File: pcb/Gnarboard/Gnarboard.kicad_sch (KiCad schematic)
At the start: 11 parts, among them J2 I2C, J3 Screw_Terminal_01x12, J4 Screw_Terminal_01x12, U2 MCP3208, U4 D24V5F3

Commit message: bill of materials updated.
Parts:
- C1: Vendor (none) -> 08053C104KAT4A
- D1: Vendor (none) -> 771-BZT52H-A30-QX
- DFR0570: renamed from U3; Vendor (none) -> 426-DFR0570
- J2: Vendor (none) -> 485-4328
- J3, J4: Vendor (none) -> BSS 2301
- JP1, JP2, U4: now left out of the parts list
- U1: value ~ -> ESP32-DEVKITC; Vendor (none) -> 356-ESP32-DEVKITC32E
- U2: Vendor (none) -> MCP3208T-BI/SL
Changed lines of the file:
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@@
   )
   (symbol (lib_id "Jumper:SolderJumper_2_Bridged") (at 34.29 73.66 0) (unit 1)
-    (in_bom yes) (on_board yes) (dnp no) (fields_autoplaced)
+    (in_bom no) (on_board yes) (dnp no) (fields_autoplaced)
     (property "Reference" "JP2" (at 34.29 67.31 0)
       (effects (font (size 1.27 1.27)))
@@
     )
     (property "Datasheet" "~" (at 95.25 35.56 0)
+      (effects (font (size 1.27 1.27)) hide)
+    )
+    (property "Vendor" "08053C104KAT4A" (at 95.25 35.56 0)
       (effects (font (size 1.27 1.27)) hide)
     )
@@
     )
     (property "Datasheet" "http://ww1.microchip.com/downloads/en/DeviceDoc/21298c.pdf" (at 207.01 59.69 0)
+      (effects (font (size 1.27 1.27)) hide)
+    )
+    (property "Vendor" "MCP3208T-BI/SL" (at 209.55 62.23 0)
       (effects (font (size 1.27 1.27)) hide)
     )
@@
       (effects (font (size 1.27 1.27)) hide)
     )
+    (property "Vendor" "771-BZT52H-A30-QX" (at 52.07 35.56 0)
+      (effects (font (size 1.27 1.27)) hide)
+    )
     (pin "1")
     (pin "2")
@@
     )
     (property "Datasheet" "~" (at 22.86 120.65 0)
+      (effects (font (size 1.27 1.27)) hide)
+    )
+    (property "Vendor" "BSS 2301" (at 22.86 120.65 0)
       (effects (font (size 1.27 1.27)) hide)
     )
@@
   )
   (symbol (lib_id "Jumper:SolderJumper_2_Bridged") (at 50.8 73.66 0) (unit 1)
-    (in_bom yes) (on_board yes) (dnp no) (fields_autoplaced)
+    (in_bom no) (on_board yes) (dnp no) (fields_autoplaced)
     (property "Reference" "JP1" (at 50.8 67.31 0)
       (effects (font (size 1.27 1.27)))
@@
   (symbol (lib_id "gnarboard:DFR0571") (at 74.93 35.56 0) (unit 1)
     (in_bom yes) (on_board yes) (dnp no) (fields_autoplaced)
-    (property "Reference" "U3" (at 74.93 25.4 0)
+    (property "Reference" "DFR0570" (at 74.93 25.4 0)
       (effects (font (size 1.27 1.27)))
     )
@@
     )
     (property "Datasheet" "" (at 74.93 26.67 0)
+      (effects (font (size 1.27 1.27)) hide)
+    )
+    (property "Vendor" "426-DFR0570 " (at 74.93 35.56 0)
       (effects (font (size 1.27 1.27)) hide)
     )
@@
       (project "Gnarboard"
         (path "/c83c6236-96e9-46ad-9d7a-9e2efa4a7966"
-          (reference "U3") (unit 1)
+          (reference "DFR0570") (unit 1)
         )
       )
@@
     )
     (property "Datasheet" "~" (at 22.86 156.21 0)
+      (effects (font (size 1.27 1.27)) hide)
+    )
+    (property "Vendor" "BSS 2301" (at 22.86 156.21 0)
       (effects (font (size 1.27 1.27)) hide)
     )
@@
       (effects (font (size 1.27 1.27)) hide)
     )
+    (property "Vendor" "485-4328" (at 271.78 54.61 0)
+      (effects (font (size 1.27 1.27)) hide)
+    )
     (pin "1")
     (pin "2")
@@
   )
   (symbol (lib_id "gnarboard:ESP32_DevKit_C") (at 156.21 66.04 0) (unit 1)
-    (in_bom yes) (on_board yes) (dnp no) (fields_autoplaced)
+    (in_bom yes) (on_board yes) (dnp no)
     (property "Reference" "U1" (at 156.21 38.1 0)
       (effects (font (size 1.27 1.27)))
     )
-    (property "Value" "~" (at 156.21 39.37 0)
-      (effects (font (size 1.27 1.27)))
+    (property "Value" "ESP32-DEVKITC" (at 156.21 41.91 0)
+      (effects (font (size 1.27 1.27)) hide)
     )
     (property "Footprint" "PCM_Espressif:ESP32-DevKitC" (at 156.21 39.37 0)
@@
     )
     (property "Datasheet" "" (at 156.21 39.37 0)
+      (effects (font (size 1.27 1.27)) hide)
+    )
+    (property "Vendor" "356-ESP32-DEVKITC32E " (at 156.21 66.04 0)
       (effects (font (size 1.27 1.27)) hide)
     )
@@
   )
   (symbol (lib_id "gnarboard:DF24V5Fx") (at 74.93 57.15 0) (unit 1)
-    (in_bom yes) (on_board yes) (dnp no) (fields_autoplaced)
+    (in_bom no) (on_board yes) (dnp no) (fields_autoplaced)
     (property "Reference" "U4" (at 74.93 49.53 0)
       (effects (font (size 1.27 1.27)))

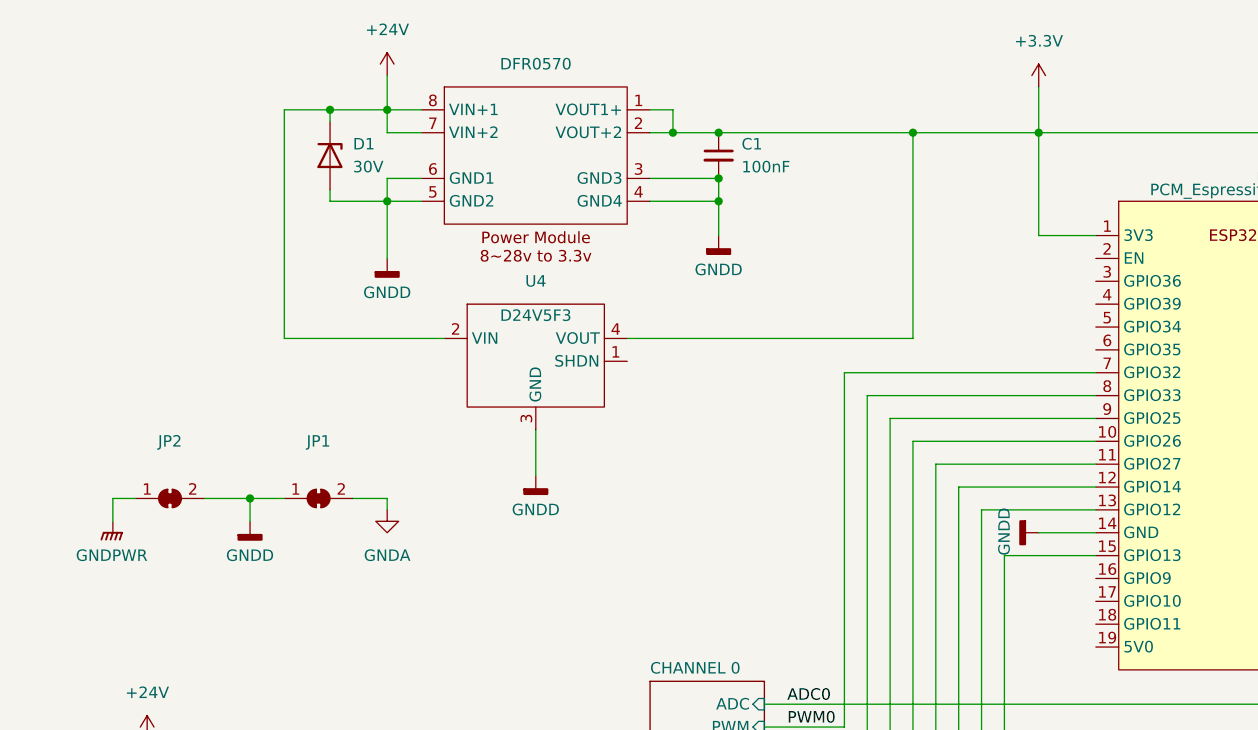
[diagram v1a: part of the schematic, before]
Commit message: added bus voltage reading functionality
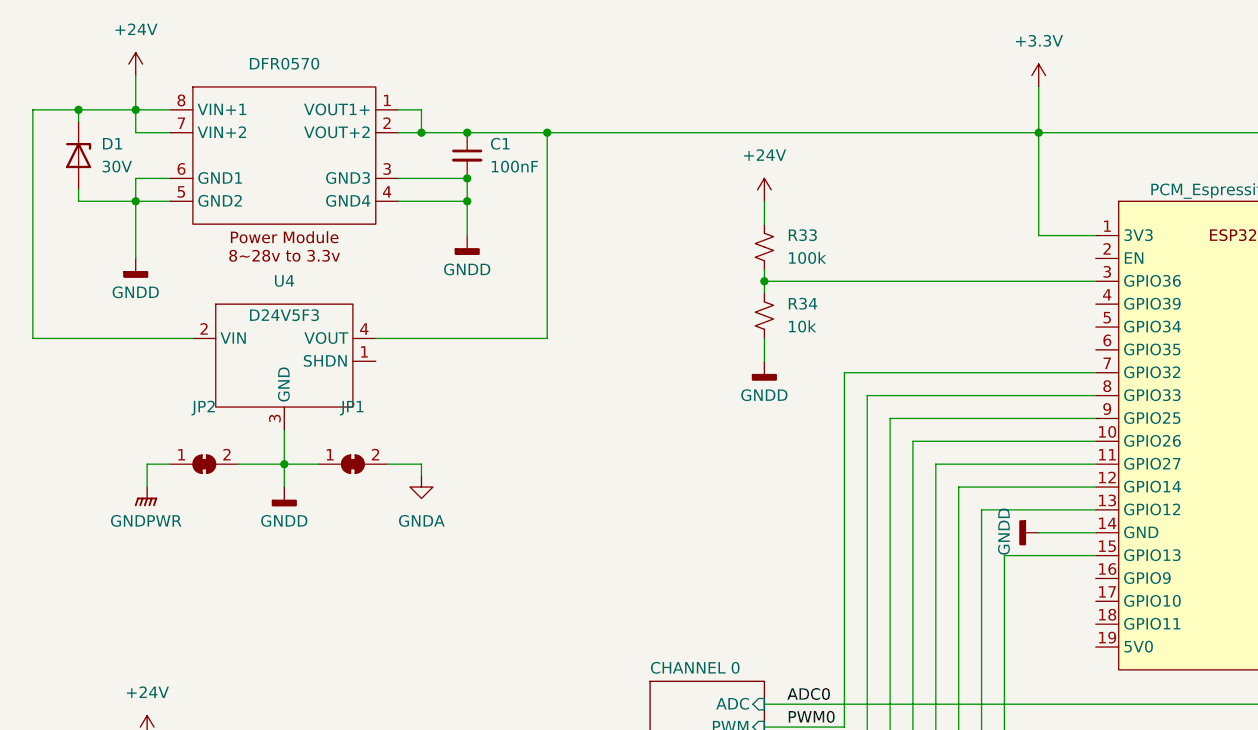
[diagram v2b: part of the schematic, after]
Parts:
- added R33: 100k, Resistor_SMD:R_0805_2012Metric_Pad1.20x1.40mm_HandSolder, symbol Device:R_Small_US
- added R34: 10k, Resistor_SMD:R_0805_2012Metric_Pad1.20x1.40mm_HandSolder, symbol Device:R_Small_US
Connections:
- net +24V: now also R33.2
- net GNDD: now also R34.1
- net at U1.3 (GPIO36): now also R33.1, R34.2
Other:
- moved on the sheet: C1, D1, DFR0570, JP1, JP2, U4

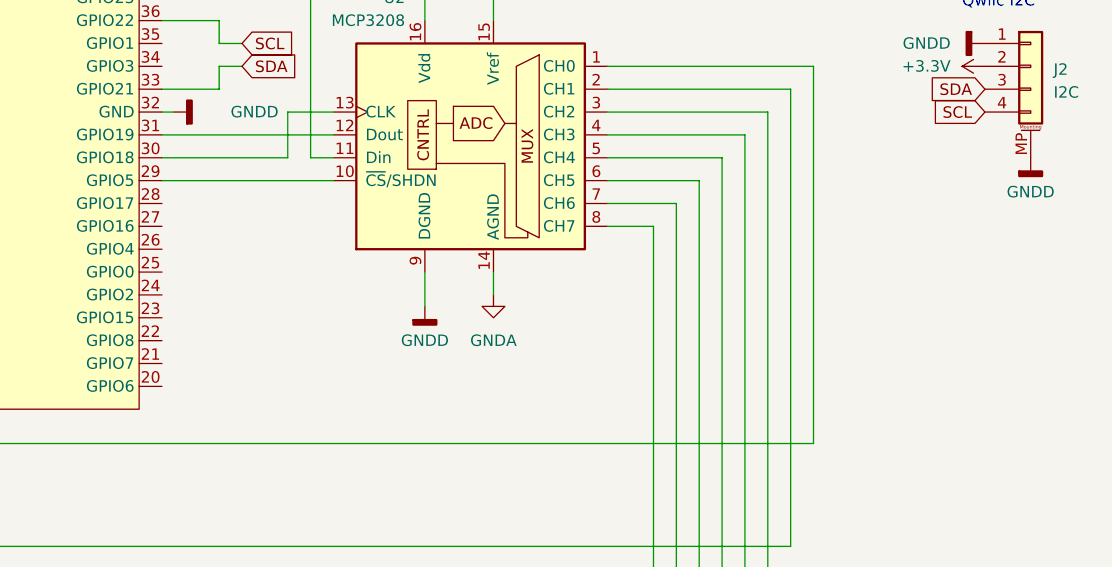
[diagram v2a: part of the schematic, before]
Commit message: got the mosfet driver circuit sorted - zener to the rescue.  also added the CAN/N2K header.
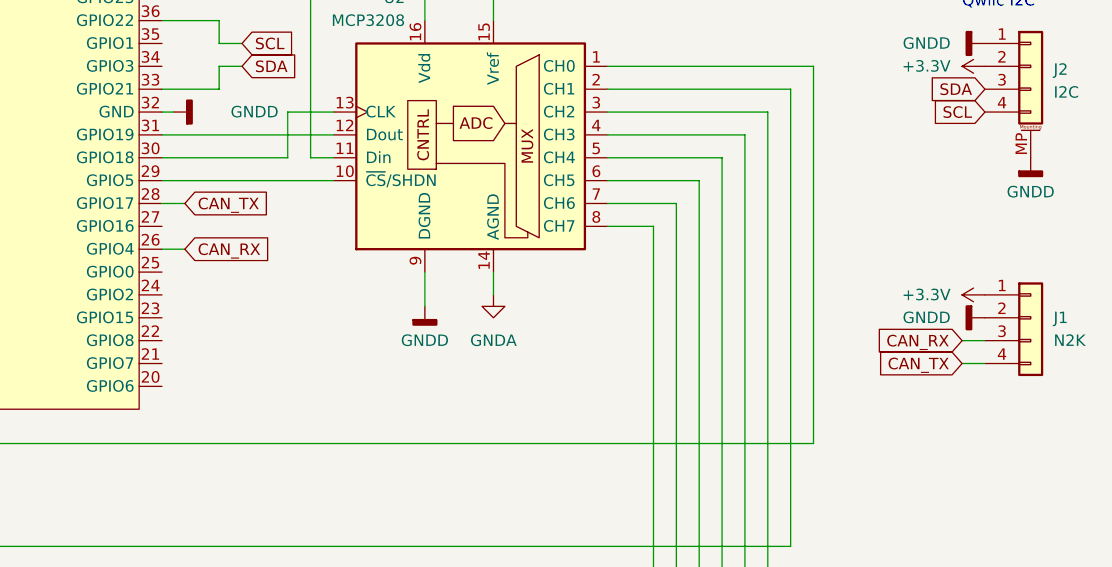
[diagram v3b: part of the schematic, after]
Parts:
- added J1: N2K, Connector_PinSocket_2.54mm:PinSocket_1x04_P2.54mm_Vertical, symbol Connector_Generic:Conn_01x04
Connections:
- net +3.3V: now also J1.1 (Pin_1)
- net GNDD: now also J1.2 (Pin_2)
- net CAN_RX: now reaches U1.26 (GPIO4)
- net CAN_RX: now also J1.3 (Pin_3)
- net CAN_TX: now reaches U1.28 (GPIO17)
- net CAN_TX: now also J1.4 (Pin_4)

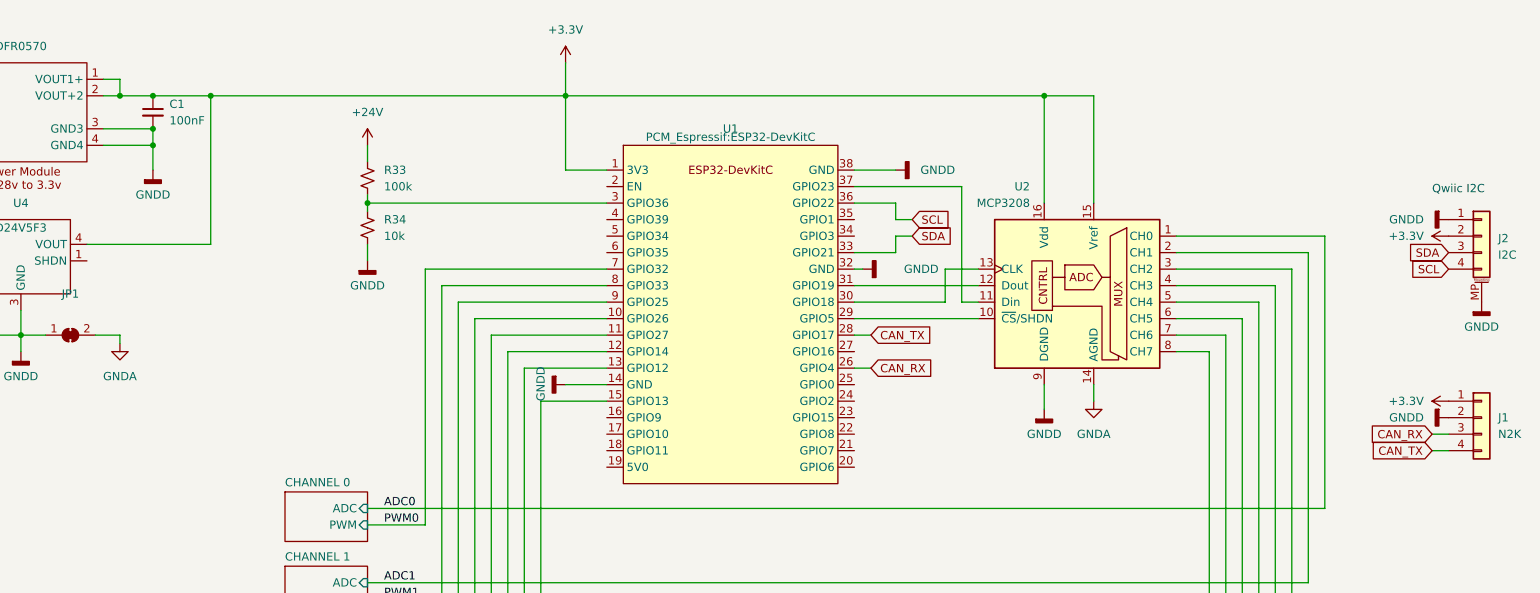
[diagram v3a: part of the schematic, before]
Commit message: updated the pin selections and changed back to using a 5v regulator.
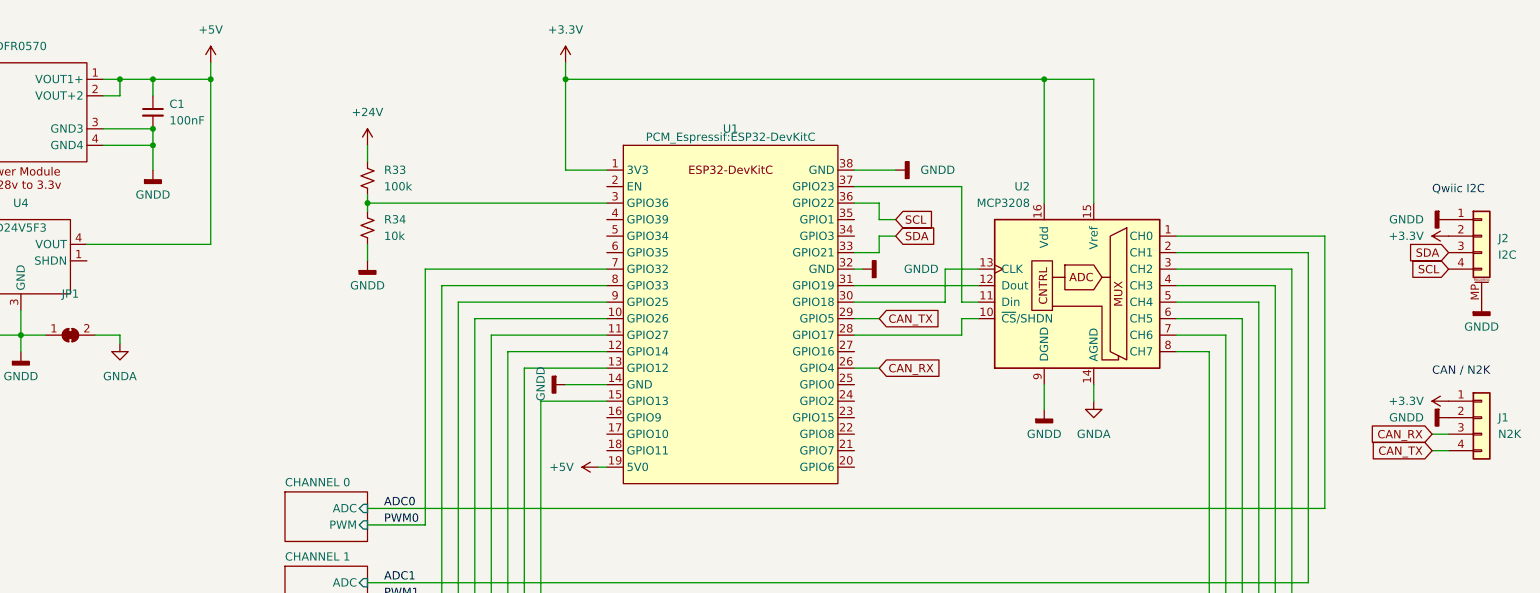
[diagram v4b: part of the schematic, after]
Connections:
- net +3.3V: no longer C1.1, DFR0570.1 (VOUT1+), DFR0570.2 (VOUT+2), U4.4 (VOUT)
- net CAN_TX: now also U1.29 (GPIO5); no longer U1.28 (GPIO17)
- net at U2.10 (~{CS}/SHDN): now also U1.28 (GPIO17); no longer U1.29 (GPIO5)
- net +5V: now reaches U1.19 (5V0)
- net +5V: now also C1.1, DFR0570.1 (VOUT1+), DFR0570.2 (VOUT+2), U4.4 (VOUT)
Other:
- note added: "CAN / N2K"

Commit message: a couple tweaks to the board
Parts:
- D1: footprint Diode_SMD:D_SOD-123 -> Diode_SMD:D_SOD-123F
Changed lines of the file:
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@@
   (paper "A4")
   (title_block
-    (rev "1.0.0")
+    (rev "A")
   )
   (junction (at 31.75 151.13) (diameter 0) (color 0 0 0 0)
@@
       (effects (font (size 1.27 1.27)) (justify left))
     )
-    (property "Footprint" "Diode_SMD:D_SOD-123" (at 19.685 35.56 0)
-      (effects (font (size 1.27 1.27)) hide)
-    )
+    (property "Footprint" "Diode_SMD:D_SOD-123F" (at 19.685 35.56 0)
+      (effects (font (size 1.27 1.27)) hide)
+    )

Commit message: went over components again, should be ready to rock and roll!
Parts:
- DFR0571: renamed from DFR0570; Vendor 426-DFR0570 -> 426-DFR0571
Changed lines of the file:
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@@
   (symbol (lib_id "gnarboard:DFR0571") (at 46.99 35.56 0) (unit 1)
     (in_bom yes) (on_board yes) (dnp no) (fields_autoplaced)
-    (property "Reference" "DFR0570" (at 46.99 25.4 0)
+    (property "Reference" "DFR0571" (at 46.99 25.4 0)
       (effects (font (size 1.27 1.27)))
     )
@@
       (effects (font (size 1.27 1.27)) hide)
     )
-    (property "Vendor" "426-DFR0570 " (at 46.99 35.56 0)
+    (property "Vendor" "426-DFR0571" (at 46.99 35.56 0)
       (effects (font (size 1.27 1.27)) hide)
     )
@@
       (project "Gnarboard"
         (path "/c83c6236-96e9-46ad-9d7a-9e2efa4a7966"
-          (reference "DFR0570") (unit 1)
+          (reference "DFR0571") (unit 1)
         )
       )

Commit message: pcb stuff
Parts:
- added J13: Screw_Terminal_01x16, symbol Connector:Screw_Terminal_01x16
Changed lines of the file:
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@@
+    )
+  )
+  (symbol (lib_id "Connector:Screw_Terminal_01x16") (at 320.04 129.54 0) (unit 1)
+    (in_bom yes) (on_board yes) (dnp no) (fields_autoplaced)
+    (property "Reference" "J13" (at 322.58 129.54 0)
+      (effects (font (size 1.27 1.27)) (justify left))
+    )
+    (property "Value" "Screw_Terminal_01x16" (at 322.58 132.08 0)
+      (effects (font (size 1.27 1.27)) (justify left))
+    )
+    (property "Footprint" "" (at 320.04 129.54 0)
+      (effects (font (size 1.27 1.27)) hide)
+    )
+    (property "Datasheet" "~" (at 320.04 129.54 0)
+      (effects (font (size 1.27 1.27)) hide)
+    )
+    (pin "1")
+    (pin "10")
+    (pin "11")
+    (pin "12")
+    (pin "13")
+    (pin "14")
+    (pin "15")
+    (pin "16")
+    (pin "2")
+    (pin "3")
+    (pin "4")
+    (pin "5")
+    (pin "6")
+    (pin "7")
+    (pin "8")
+    (pin "9")
+    (instances
+      (project "Gnarboard"
+        (path "/c83c6236-96e9-46ad-9d7a-9e2efa4a7966"
+          (reference "J13") (unit 1)
+        )
+      )
     )
   )

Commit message: more progress, found a nice easy regulator too.
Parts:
- removed D1: 30V, Diode_SMD:D_SOD-123F, symbol Diode:ZPDxx
- removed DFR0571: ~, gnarboard:DF1768, symbol gnarboard:DFR0571
- removed J13: Screw_Terminal_01x16, symbol Connector:Screw_Terminal_01x16
- removed U4: D24V5F3, gnarboard:D24V5FX, symbol gnarboard:DF24V5Fx
- added C2: 10uF, Capacitor_SMD:C_0805_2012Metric_Pad1.18x1.45mm_HandSolder, symbol Device:C_Small
- added C27: 1nF, Capacitor_SMD:C_0805_2012Metric_Pad1.18x1.45mm_HandSolder, symbol Device:C_Small
- added D18: BZX384, Diode_SMD:D_SOD-323_HandSoldering, symbol Device:D_Zener
- added L1: 100uH, Inductor_SMD:L_1210_3225Metric_Pad1.42x2.65mm_HandSolder, symbol Device:L
- added U3: R-78B3.3-2.0, Converter_DCDC:Converter_DCDC_RECOM_R-78B-2.0_THT, symbol Regulator_Switching:R-78B3.3-2.0
- C1: value 100nF -> 10uF
- J1: footprint Connector_PinSocket_2.54mm:PinSocket_1x04_P2.54mm_Vertical -> Connector_PinSocket_2.54mm:PinSocket_1x04_P2.54mm_Horizontal
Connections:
- net +24V: now also C1.1, L1.1
- net +5V: now also D18.1 (K); no longer C1.1
- net GNDD: now also C2.2, U3.2 (GND)
- new net: C2.1, C27.1, L1.2, U3.1 (IN)
- new net: C27.2, D18.2 (A), U3.3 (OUT)
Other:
- moved on the sheet: C1, JP1, JP2
